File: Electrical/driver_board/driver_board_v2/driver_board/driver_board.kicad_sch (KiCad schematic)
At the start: 0 parts

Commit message: Updates to driver board
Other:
- added sheet PSU (power-supply.kicad_sch)
- sheet MCU: file untitled.kicad_sch -> microcontroller.kicad_sch
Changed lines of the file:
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@@
 			)
 		)
-		(property "Sheetfile" "untitled.kicad_sch"
+		(property "Sheetfile" "microcontroller.kicad_sch"
 			(at 60.96 89.4846 0)
 			(effects
@@
 				)
 			)
+		)
+	)
+	(sheet
+		(at 119.38 68.58)
+		(size 43.18 20.32)
+		(exclude_from_sim no)
+		(in_bom yes)
+		(on_board yes)
+		(dnp no)
+		(fields_autoplaced yes)
+		(stroke
+			(width 0.1524)
+			(type solid)
+		)
+		(fill
+			(color 0 0 0 0.0000)
+		)
+		(property "Sheetname" "PSU"
+			(at 119.38 67.8684 0)
+			(effects
+				(font
+					(size 1.27 1.27)
+				)
+				(justify left bottom)
+			)
+		)
+		(property "Sheetfile" "power-supply.kicad_sch"
+			(at 119.38 89.4846 0)
+			(effects
+				(font
+					(size 1.27 1.27)
+				)
+				(justify left top)
+			)
+		)
+		(instances
+			(project "driver_board"
+				(path "/914a9dfd-cc72-459d-a4b5-1249c31e6215"
+					(page "3")
+				)
+			)

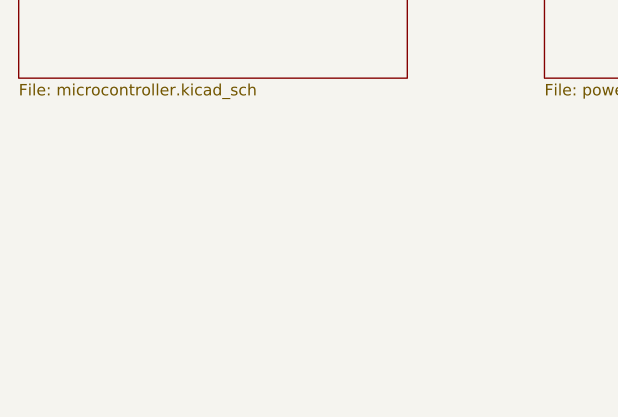
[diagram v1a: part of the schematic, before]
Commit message: Added footprint of motor driver and added power
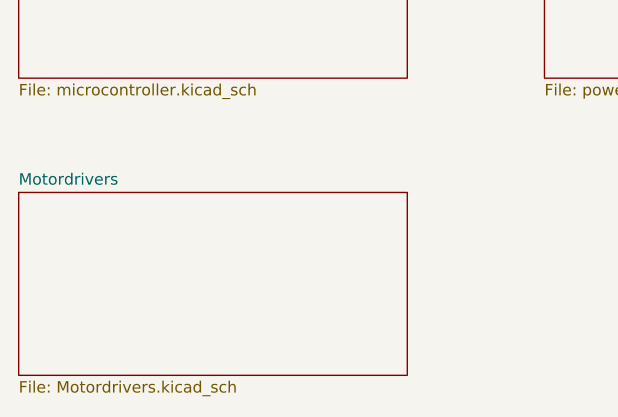
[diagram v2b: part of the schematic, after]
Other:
- added sheet Motordrivers (Motordrivers.kicad_sch)
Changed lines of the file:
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@@
 	(paper "A4")
+	(sheet
+		(at 60.96 101.6)
+		(size 43.18 20.32)
+		(exclude_from_sim no)
+		(in_bom yes)
+		(on_board yes)
+		(dnp no)
+		(fields_autoplaced yes)
+		(stroke
+			(width 0.1524)
+			(type solid)
+		)
+		(fill
+			(color 0 0 0 0.0000)
+		)
+		(property "Sheetname" "Motordrivers"
+			(at 60.96 100.8884 0)
+			(effects
+				(font
+					(size 1.27 1.27)
+				)
+				(justify left bottom)
+			)
+		)
+		(property "Sheetfile" "Motordrivers.kicad_sch"
+			(at 60.96 122.5046 0)
+			(effects
+				(font
+					(size 1.27 1.27)
+				)
+				(justify left top)
+			)
+		)
+		(instances
+			(project "driver_board"
+				(path "/914a9dfd-cc72-459d-a4b5-1249c31e6215"
+					(page "4")
+				)
+			)
+		)
+	)
 	(sheet
 		(at 60.96 68.58)

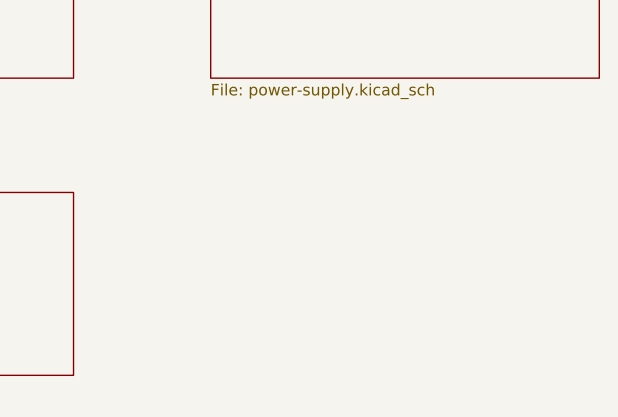
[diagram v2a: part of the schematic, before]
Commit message: Discovered critical error and changed pinout
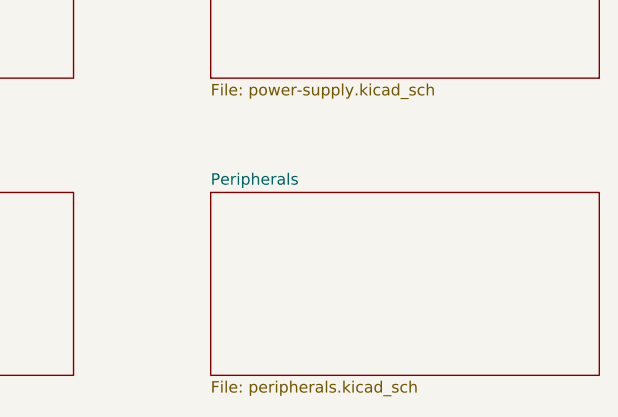
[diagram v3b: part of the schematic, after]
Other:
- added sheet Peripherals (peripherals.kicad_sch)
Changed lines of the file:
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@@
+	)
+	(sheet
+		(at 119.38 101.6)
+		(size 43.18 20.32)
+		(exclude_from_sim no)
+		(in_bom yes)
+		(on_board yes)
+		(dnp no)
+		(fields_autoplaced yes)
+		(stroke
+			(width 0.1524)
+			(type solid)
+		)
+		(fill
+			(color 0 0 0 0.0000)
+		)
+		(property "Sheetname" "Peripherals"
+			(at 119.38 100.8884 0)
+			(effects
+				(font
+					(size 1.27 1.27)
+				)
+				(justify left bottom)
+			)
+		)
+		(property "Sheetfile" "peripherals.kicad_sch"
+			(at 119.38 122.5046 0)
+			(effects
+				(font
+					(size 1.27 1.27)
+				)
+				(justify left top)
+			)
+		)
+		(instances
+			(project "driver_board"
+				(path "/914a9dfd-cc72-459d-a4b5-1249c31e6215"
+					(page "5")
+				)
+			)
+		)
 	)
 	(sheet

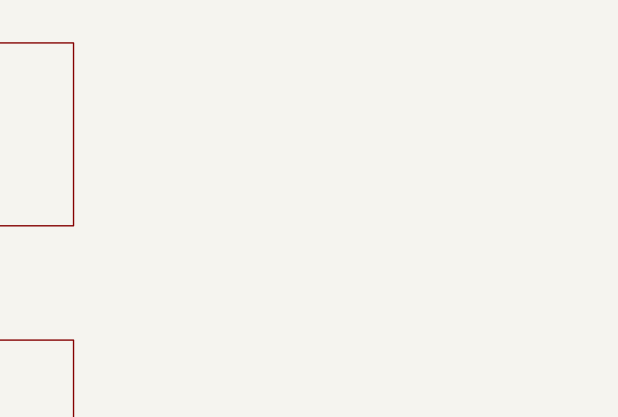
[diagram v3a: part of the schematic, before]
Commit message: Added gripper
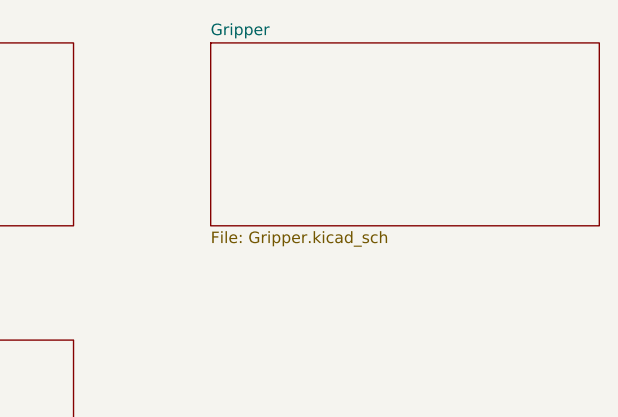
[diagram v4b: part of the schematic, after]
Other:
- added sheet Gripper (Gripper.kicad_sch)
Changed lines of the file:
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@@
 	(paper "A4")
+	(sheet
+		(at 177.8 68.58)
+		(size 43.18 20.32)
+		(exclude_from_sim no)
+		(in_bom yes)
+		(on_board yes)
+		(dnp no)
+		(fields_autoplaced yes)
+		(stroke
+			(width 0.1524)
+			(type solid)
+		)
+		(fill
+			(color 0 0 0 0.0000)
+		)
+		(property "Sheetname" "Gripper"
+			(at 177.8 67.8684 0)
+			(effects
+				(font
+					(size 1.27 1.27)
+				)
+				(justify left bottom)
+			)
+		)
+		(property "Sheetfile" "Gripper.kicad_sch"
+			(at 177.8 89.4846 0)
+			(effects
+				(font
+					(size 1.27 1.27)
+				)
+				(justify left top)
+			)
+		)
+		(instances
+			(project "driver_board"
+				(path "/914a9dfd-cc72-459d-a4b5-1249c31e6215"
+					(page "6")
+				)
+			)
+		)
+	)
 	(sheet
 		(at 60.96 101.6)
